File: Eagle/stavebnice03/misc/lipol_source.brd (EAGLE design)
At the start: 21 x 21 mm, 27 parts

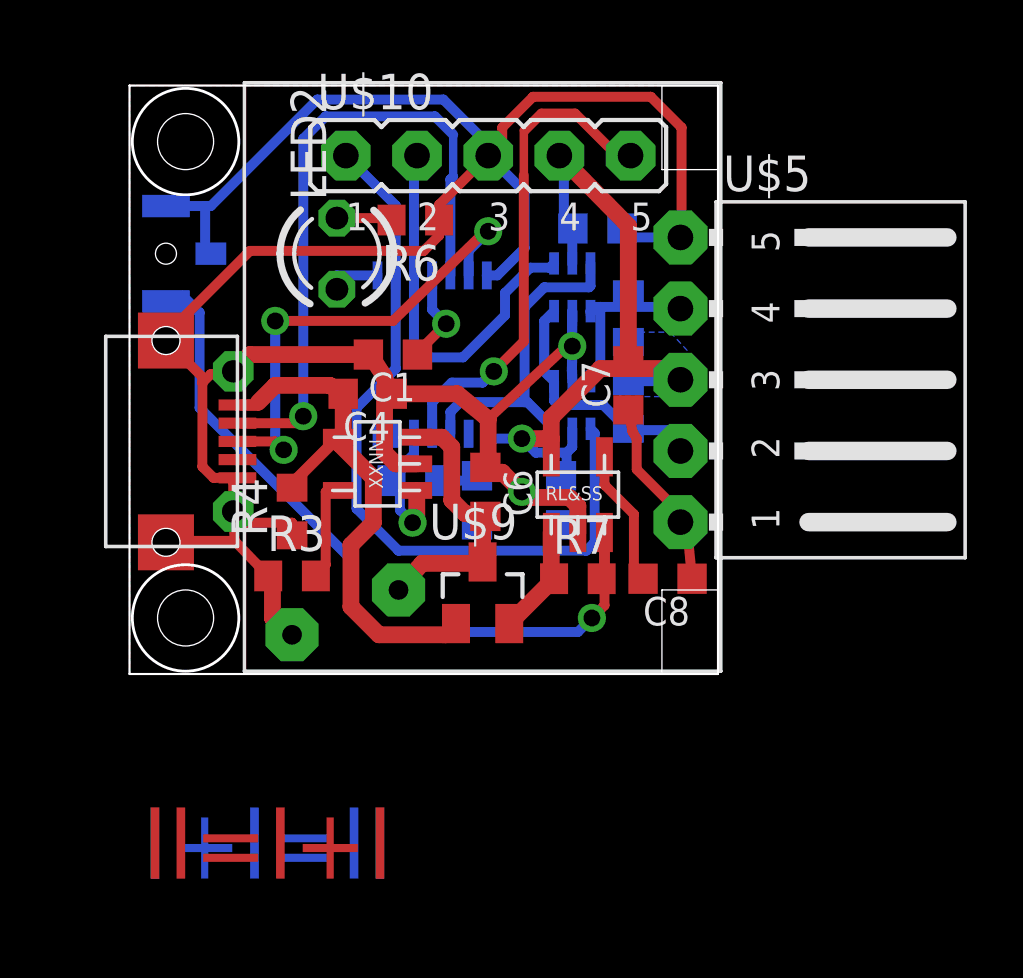
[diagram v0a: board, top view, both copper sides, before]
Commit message: layer coloring and place drawing moved to docu layer + changed sizes of names and values
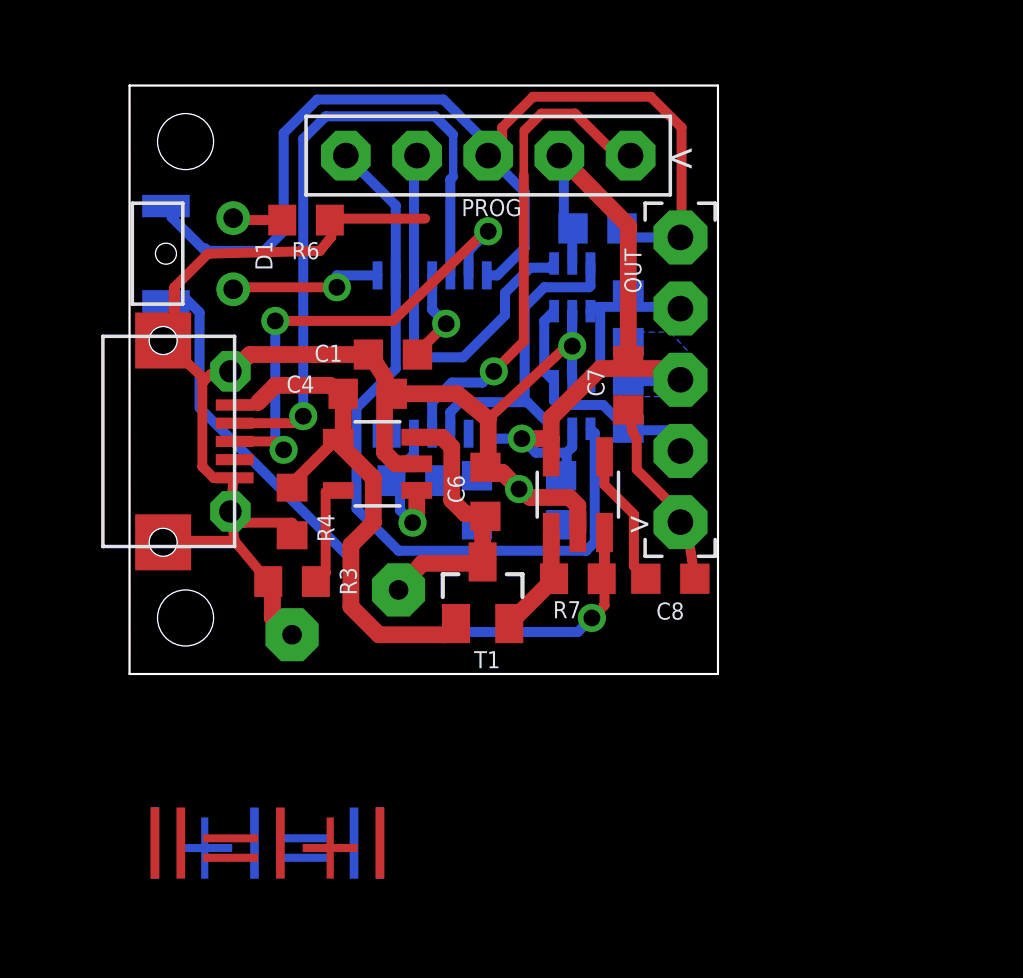
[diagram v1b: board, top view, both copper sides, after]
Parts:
- removed LED2: (no value), led:LED3MM
- removed U$2: USBMICRO, !stavebnice03:MICROUSB-MOLEX
- added D1: LED1.8, !stavebnice03:LED1.8
- added USB: USBMICRO, !stavebnice03:MICROUSB-MOLEX
- C7: value 4,7uF -> 4.7uF
- R5: value 10k -> 100k
- T1: value P-MOSFET-FDV304P -> FDV304P
- moved R6 3.90 mm to (6.30, 16.2)
- moved R3 0.20 mm to (5.80, 3.30)
- moved C8 0.10 mm to (19.3, 3.40)
- turned PROG to 180 degrees
- renumbered NC7SB3157P6X(1) to U3, NC7SB3157P6X(2) to U2, U$1 to U1, U$10 to PROG, U$5 to OUT, U$9 to T1
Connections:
- net GND: now also USB.GND, USB.NC, USB.P$1, USB.P$2, USB.P$3, USB.P$6; no longer U$2.GND, U$2.P$1, U$2.P$2, U$2.P$3, U$2.P$6, U$6.P$3
- net N$14: now also PROG.1; no longer PROG.5
- net N$15: now also D1.K; no longer LED2.K
- net N$16: now also D1.A; no longer LED2.A
- net N$2: now also USB.D-; no longer U$2.D-
- net N$4: now also PROG.4; no longer PROG.2
- net N$5: now also USB.D+; no longer U$2.D+
- net N$7: now also PROG.5; no longer PROG.1
- net N$9: now also USB.VUSB; no longer U$2.VUSB
- net VCC: now also PROG.2; no longer PROG.4
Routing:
- net N$16: track 1.95 -> 6.25 mm, vias 0 -> 1
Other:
- outline, holes or cut-outs redrawn

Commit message: added bootloder touch point and pull up resistor to switcher + increased interface led resistor, it lighted too much
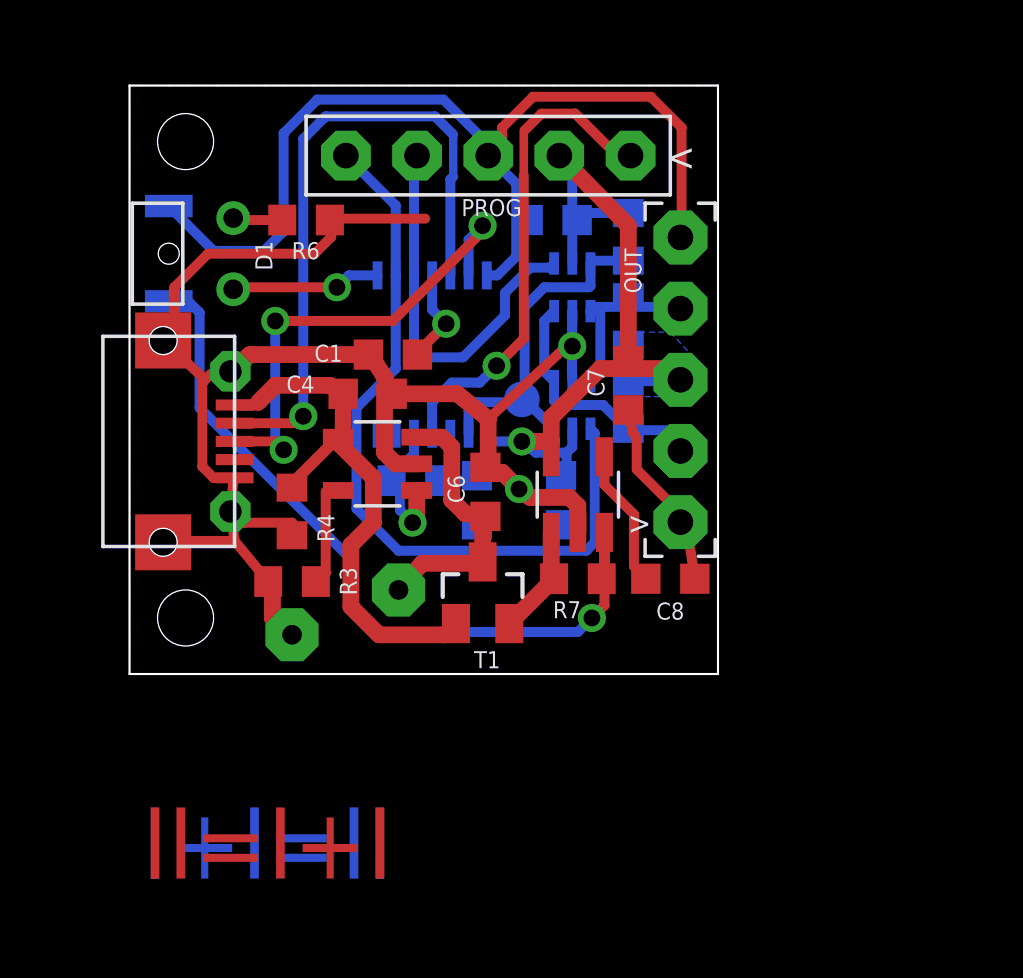
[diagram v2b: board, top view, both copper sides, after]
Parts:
- removed U$6: BYTTON-B3U, !stavebnice03:BUTTON-B3U
- added R8: 100k, resistor:R0603
- added RESET: BYTTON-B3U, !stavebnice03:BUTTON-B3U
- added TP1: TPB1,27, testpad:B1,27
- R6: value 100 -> 2k2
- moved C3 1.63 mm to (15.1, 16.2), turned to 180 degrees
- moved R2 0.10 mm to (17.8, 12.6)
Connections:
- net GND: now also RESET.P$1; no longer U$6.P$1
- net N$1: now also R8.2, TP1.TP, U1.2; no longer U1.3
- net N$20: now also RESET.P$2; no longer U$6.P$2
- net VCC: now also R8.1
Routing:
- net VCC: track 33.0 -> 36.4 mm
- net GND: track 109.2 -> 106.2 mm
- net N$16: track 6.25 -> 5.36 mm
- net N$1: track 11.9 -> 12.7 mm
- net N$15: track 2.46 -> 1.82 mm

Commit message: eagle adjustment for the Jíťa version
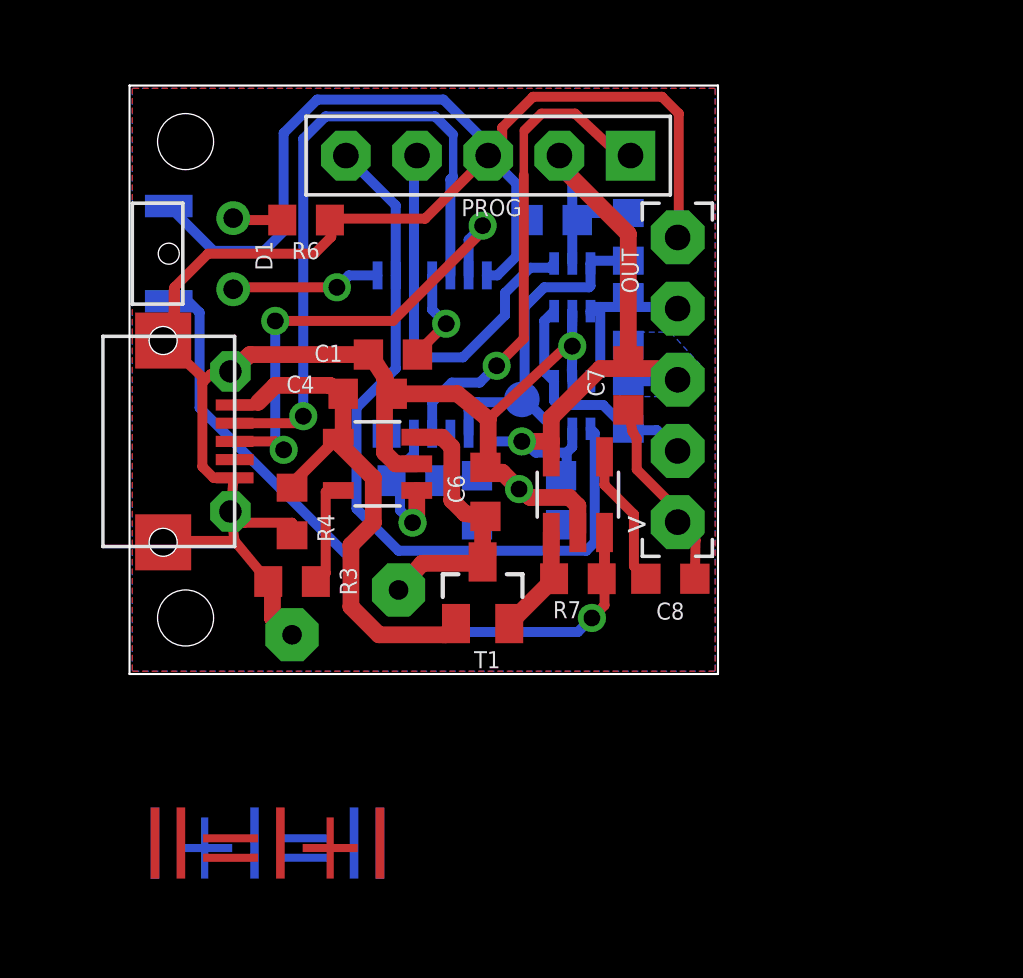
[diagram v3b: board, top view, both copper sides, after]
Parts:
- moved OUT 0.10 mm to (22.1, 10.5)
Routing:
- net GND: track 106.2 -> 109.8 mm
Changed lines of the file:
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@@
 <layer number="27" name="tValues" color="3" fill="1" visible="no" active="yes"/>
 <layer number="28" name="bValues" color="7" fill="1" visible="no" active="yes"/>
-<layer number="29" name="tStop" color="7" fill="3" visible="no" active="yes"/>
-<layer number="30" name="bStop" color="7" fill="6" visible="no" active="yes"/>
+<layer number="29" name="tStop" color="7" fill="3" visible="yes" active="yes"/>
+<layer number="30" name="bStop" color="7" fill="6" visible="yes" active="yes"/>
 <layer number="31" name="tCream" color="7" fill="4" visible="no" active="yes"/>
 <layer number="32" name="bCream" color="7" fill="5" visible="no" active="yes"/>
@@
 <param name="mnLayersViaInSmd" value="2"/>
 <param name="mdCopperDimension" value="0mil"/>
-<param name="mdDrill" value="8mil"/>
+<param name="mdDrill" value="1mil"/>
 <param name="mdSmdStop" value="0mil"/>
 <param name="msWidth" value="10mil"/>
-<param name="msDrill" value="23mil"/>
+<param name="msDrill" value="0.015240625mm"/>
 <param name="msMicroVia" value="9.99mm"/>
 <param name="msBlindViaRatio" value="0.5"/>
@@
 <param name="mlMinCreamFrame" value="0mil"/>
 <param name="mlMaxCreamFrame" value="0mil"/>
-<param name="mlViaStopLimit" value="7mm"/>
+<param name="mlViaStopLimit" value="0.7mm"/>
 <param name="srRoundness" value="0"/>
 <param name="srMinRoundness" value="0mil"/>
@@
 <attribute name="VALUE" x="14.3" y="16.45" size="0.4064" layer="28" ratio="10" rot="MR180"/>
 </element>
-<element name="OUT" library="!stavebnice03" package="JUMPER5F-90" value="JUMPER5F-90" x="22.2" y="10.5" smashed="yes" rot="R270">
-<attribute name="NAME" x="18.269" y="13.584" size="0.6096" layer="25" ratio="15" rot="R90"/>
+<element name="OUT" library="!stavebnice03" package="JUMPER5F-90" value="JUMPER5F-90" x="22.1" y="10.5" smashed="yes" rot="R270">
+<attribute name="NAME" x="18.169" y="13.584" size="0.6096" layer="25" ratio="15" rot="R90"/>
 </element>
 <element name="U3" library="!stavebnice03" package="SC70-6L" value="NC7SB3157P6X" x="15.8" y="9.6" smashed="yes" rot="MR180">
@@
 <wire x1="15.7875" y1="10.7875" x2="15.8" y2="11.7" width="0.357" layer="16"/>
 <via x="15.8" y="11.7" extent="1-16" drill="0.6"/>
-<polygon width="0.01" layer="16" isolate="0.41" thermals="no" rank="2">
-<vertex x="0" y="0"/>
-<vertex x="0" y="21"/>
-<vertex x="21" y="21"/>
-<vertex x="21" y="0"/>
+<polygon width="0.2" layer="16" isolate="0.41" thermals="no" rank="2">
+<vertex x="0.1" y="0.1"/>
+<vertex x="0.1" y="20.9"/>
+<vertex x="20.9" y="20.9"/>
+<vertex x="20.9" y="0.1"/>
 </polygon>
 <wire x1="15.8" y1="12.95" x2="15.7875" y2="11.7125" width="0.357" layer="16"/>
@@
 <contactref element="C1" pad="2"/>
 <wire x1="3.6" y1="10.8" x2="3.8" y2="10.65" width="0.3556" layer="1"/>
-<wire x1="19.64" y1="5.4" x2="19.66" y2="5.42" width="0.3556" layer="1"/>
+<wire x1="19.64" y1="5.4" x2="19.56" y2="5.42" width="0.3556" layer="1"/>
 <contactref element="U$3" pad="GND"/>
 <contactref element="MCP73832" pad="2"/>
@@
 <wire x1="11.7" y1="10" x2="9.375" y2="10" width="0.6" layer="1"/>
 <wire x1="9.1" y1="10.25" x2="9.375" y2="10" width="0.3556" layer="1"/>
-<wire x1="19.66" y1="15.58" x2="19.7" y2="15.58" width="0.3556" layer="16"/>
-<polygon width="0.01" layer="1" isolate="0.4" thermals="no" rank="2">
-<vertex x="0" y="0"/>
-<vertex x="21" y="0"/>
-<vertex x="21" y="21"/>
-<vertex x="0" y="21"/>
+<polygon width="0.2" layer="1" isolate="0.4" thermals="no" rank="2">
+<vertex x="0.1" y="0.1"/>
+<vertex x="20.9" y="0.1"/>
+<vertex x="20.9" y="20.9"/>
+<vertex x="0.1" y="20.9"/>
 </polygon>
 <wire x1="5.8" y1="4.95" x2="5.8" y2="5.4" width="0.3556" layer="1"/>
@@
 <via x="13.9" y="6.6" extent="1-16" drill="0.6"/>
 <wire x1="9.5" y1="7.5" x2="10.25" y2="7.5" width="0.6" layer="1"/>
-<wire x1="19.7" y1="15.68" x2="19.7" y2="19.5" width="0.3556" layer="1"/>
-<wire x1="19.7" y1="19.5" x2="18.6" y2="20.6" width="0.3556" layer="1"/>
-<wire x1="18.6" y1="20.6" x2="14.4" y2="20.6" width="0.3556" layer="1"/>
+<wire x1="19" y1="20.6" x2="14.4" y2="20.6" width="0.3556" layer="1"/>
 <wire x1="14.4" y1="20.6" x2="13.3" y2="19.5" width="0.3556" layer="1"/>
 <wire x1="13.3" y1="19.5" x2="13.3" y2="18.9" width="0.3556" layer="1"/>
-<wire x1="19.66" y1="5.42" x2="19.66" y2="5.74" width="0.3556" layer="1"/>
+<wire x1="19.56" y1="5.42" x2="19.66" y2="5.74" width="0.3556" layer="1"/>
 <wire x1="19.66" y1="5.74" x2="18.1" y2="7.3" width="0.3556" layer="1"/>
 <wire x1="18.1" y1="7.3" x2="18.1" y2="8.4" width="0.3556" layer="1"/>
 <wire x1="18.1" y1="8.4" x2="17.95" y2="8.65" width="0.3556" layer="1"/>
 <wire x1="17.95" y1="8.65" x2="17.8" y2="9.425" width="0.3556" layer="1"/>
-<wire x1="20.175" y1="3.4" x2="19.9" y2="5.18" width="0.3556" layer="1"/>
-<wire x1="19.9" y1="5.18" x2="19.66" y2="5.42" width="0.3556" layer="1"/>
+<wire x1="20.175" y1="3.4" x2="20.2" y2="4.78" width="0.3556" layer="1"/>
+<wire x1="20.2" y1="4.78" x2="19.56" y2="5.42" width="0.3556" layer="1"/>
 <wire x1="4.95" y1="3.3" x2="3.75" y2="4.75" width="0.3556" layer="1"/>
 <wire x1="3.75" y1="4.75" x2="3.6" y2="5.8" width="0.3556" layer="1"/>
@@
 <wire x1="4.8" y1="15.1" x2="5.5" y2="15.8" width="0.3556" layer="16"/>
 <wire x1="5.5" y1="19.3" x2="6.7" y2="20.5" width="0.3556" layer="16"/>
-<wire x1="10.55" y1="16.25" x2="7.2" y2="16.25" width="0.3556" layer="1"/>
 <wire x1="7.2" y1="16.25" x2="7.15" y2="16.2" width="0.3556" layer="1"/>
 <contactref element="USB" pad="NC"/>
@@
 <wire x1="4.8" y1="15.1" x2="3" y2="15.1" width="0.3556" layer="16"/>
 <wire x1="3" y1="15.1" x2="1.4" y2="16.7" width="0.3556" layer="16"/>
+<wire x1="19" y1="20.6" x2="19.6" y2="20" width="0.3556" layer="1"/>
+<wire x1="19.6" y1="20" x2="19.6" y2="15.6" width="0.3556" layer="1"/>
+<wire x1="7.2" y1="16.25" x2="10.55" y2="16.25" width="0.3556" layer="1"/>
+<wire x1="10.55" y1="16.25" x2="12.8" y2="18.5" width="0.3556" layer="1"/>
 </signal>
 <signal name="VCC">
@@
 <wire x1="12.55" y1="6.9" x2="12.4" y2="7.075" width="0.3556" layer="16"/>
 <wire x1="15.975" y1="16.2" x2="15.7" y2="15.9" width="0.3556" layer="16"/>
-<wire x1="19.51" y1="10.45" x2="19.66" y2="10.5" width="0.3556" layer="16"/>
-<wire x1="17.8" y1="16" x2="17.8" y2="11.175" width="0.6" layer="1"/>
+<wire x1="19.51" y1="10.45" x2="19.56" y2="10.5" width="0.3556" layer="16"/>
+<wire x1="17.8" y1="15.7" x2="17.8" y2="11.175" width="0.6" layer="1"/>
 <polygon width="0.1" layer="16" isolate="0.4" thermals="no">
 <vertex x="17.5" y="12.2"/>
@@
 <wire x1="15.8" y1="18" x2="15.5" y2="18.2" width="0.357" layer="16"/>
 <wire x1="16.8" y1="10.9" x2="18.2" y2="10.9" width="0.6" layer="1"/>
-<wire x1="18.2" y1="10.9" x2="19.26" y2="10.9" width="0.6" layer="1"/>
-<wire x1="19.26" y1="10.9" x2="19.66" y2="10.5" width="0.6" layer="1"/>
+<wire x1="18.2" y1="10.9" x2="19.16" y2="10.9" width="0.6" layer="1"/>
+<wire x1="19.16" y1="10.9" x2="19.56" y2="10.5" width="0.6" layer="1"/>
 <wire x1="17.8" y1="11.175" x2="17.95" y2="11.15" width="0.3556" layer="1"/>
 <wire x1="17.95" y1="11.15" x2="18.2" y2="10.9" width="0.3556" layer="1"/>
@@
 <contactref element="PROG" pad="2"/>
 <wire x1="15.5" y1="18.2" x2="15.34" y2="18.5" width="0.3556" layer="16"/>
-<wire x1="17.8" y1="16" x2="15.34" y2="18.5" width="0.6" layer="1"/>
+<wire x1="17.8" y1="15.7" x2="15.4" y2="18.1" width="0.6" layer="1"/>
+<wire x1="15.4" y1="18.1" x2="15.4" y2="18.5" width="0.6" layer="1"/>
+<wire x1="15.4" y1="18.5" x2="15.34" y2="18.5" width="0.6" layer="1"/>
 <contactref element="R8" pad="1"/>
 <wire x1="17.8" y1="16.45" x2="16.225" y2="16.45" width="0.3556" layer="16"/>
@@
 <wire x1="16.6" y1="13.1" x2="16.8" y2="13.1" width="0.3556" layer="16"/>
 <wire x1="16.8" y1="13.1" x2="17.8" y2="13.1" width="0.3556" layer="16"/>
-<wire x1="17.8" y1="13.1" x2="19.6" y2="13.1" width="0.3556" layer="16"/>
-<wire x1="19.6" y1="13.1" x2="19.66" y2="13.04" width="0.3556" layer="16"/>
+<wire x1="17.8" y1="13.1" x2="19.5" y2="13.1" width="0.3556" layer="16"/>
+<wire x1="19.5" y1="13.1" x2="19.56" y2="13.04" width="0.3556" layer="16"/>
 <wire x1="17.8" y1="13.45" x2="17.8" y2="13.1" width="0.3556" layer="16"/>
 </signal>
@@
 <wire x1="14.8" y1="10.795" x2="15.15" y2="10.45" width="0.357" layer="16"/>
 <wire x1="17.8" y1="8.75" x2="18.1" y2="8.7" width="0.3556" layer="16"/>
-<wire x1="18.1" y1="8.7" x2="19.62" y2="8.7" width="0.3556" layer="16"/>
 <wire x1="17.8" y1="8.75" x2="17.95" y2="8.75" width="0.3556" layer="16"/>
 <wire x1="17.95" y1="8.75" x2="17.9" y2="8.8" width="0.3556" layer="16"/>
@@
 <wire x1="15.15" y1="9.75" x2="15.3" y2="9.6" width="0.3556" layer="16"/>
 <wire x1="15.3" y1="9.6" x2="16.9" y2="9.6" width="0.3556" layer="16"/>
-<wire x1="19.66" y1="8.06" x2="19.66" y2="7.96" width="0.3556" layer="16"/>
-<wire x1="19.62" y1="8.7" x2="19.66" y2="8.06" width="0.3556" layer="16"/>
+<wire x1="18.1" y1="8.7" x2="18.82" y2="8.7" width="0.3556" layer="16"/>
+<wire x1="18.82" y1="8.7" x2="19.56" y2="7.96" width="0.3556" layer="16"/>
 </signal>
 <signal name="N$7">
@@
 <wire x1="14.07" y1="11.97" x2="13.1" y2="11" width="0.3556" layer="1"/>
 <wire x1="14.1" y1="19.4" x2="14.7" y2="20" width="0.357" layer="1"/>
-<wire x1="17.48" y1="18.42" x2="15.9" y2="20" width="0.3556" layer="1"/>
+<wire x1="17.48" y1="18.52" x2="15.9" y2="20" width="0.3556" layer="1"/>
 <contactref element="PROG" pad="1"/>
-<wire x1="17.88" y1="18.5" x2="17.48" y2="18.42" width="0.3556" layer="1"/>
+<wire x1="17.88" y1="18.5" x2="17.48" y2="18.52" width="0.3556" layer="1"/>
 <wire x1="14.07" y1="19.4" x2="14.1" y2="19.4" width="0" layer="19" extent="1-1"/>
 </signal>
@@
 </signal>
 </signals>
+<errors>
+</errors>
 </board>
 </drawing>
